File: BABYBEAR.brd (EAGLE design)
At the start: 68.6 x 53.3 mm, 63 parts, among them IC1 ATMEGA1284P, IC2 ATMEGA16U2-MU, IC3 MC33269DT-5.0, IC4 LM358D, IC5 LP2985-33DBVR, J1 Power, J2 Analog, J3 Digital_8_13, J4 Digital_0_7, J5 DC_2_1MM, P1 USB-6PSMT, P2 ICSP:MAIN, P3 ICSP:USB, Q1 FDN340P, Q2 2N7002, X1 16MHz, X2 16MHz

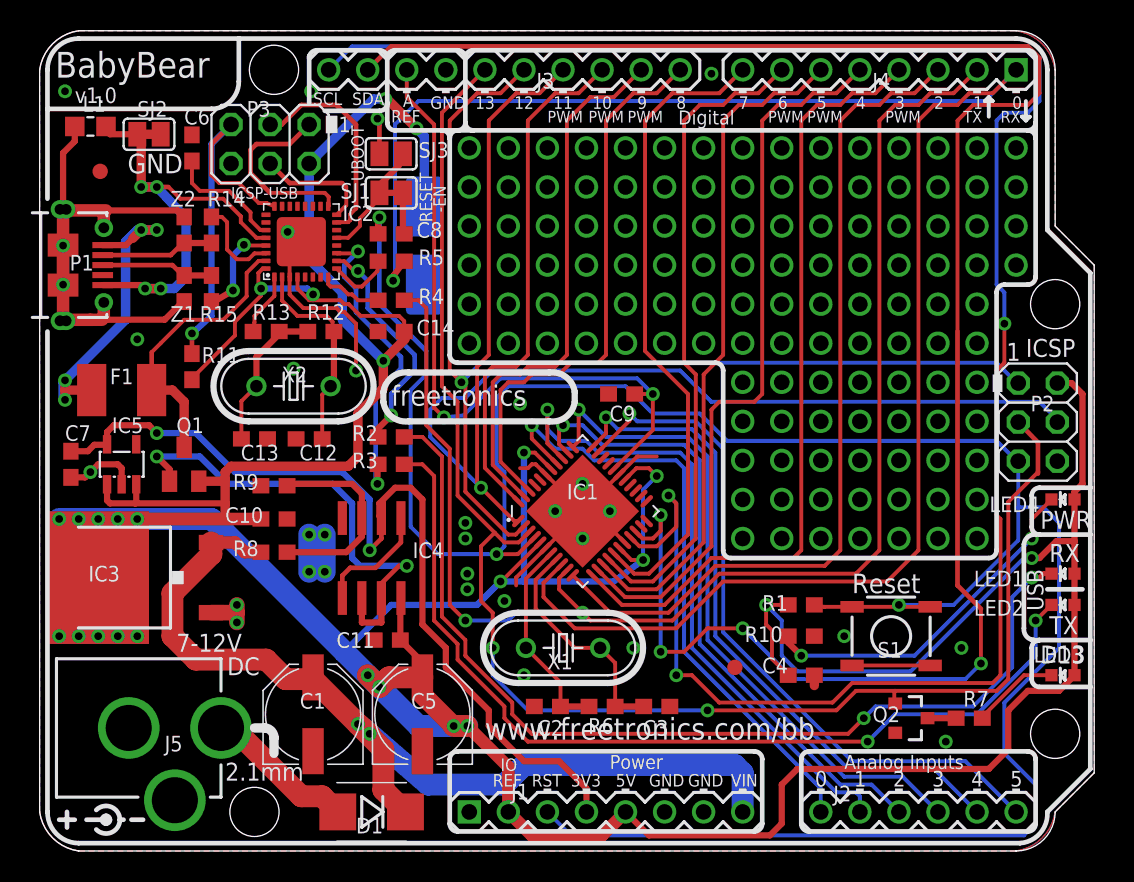
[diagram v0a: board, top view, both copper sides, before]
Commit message: Changed USB connector to USB-C for v2.0 release
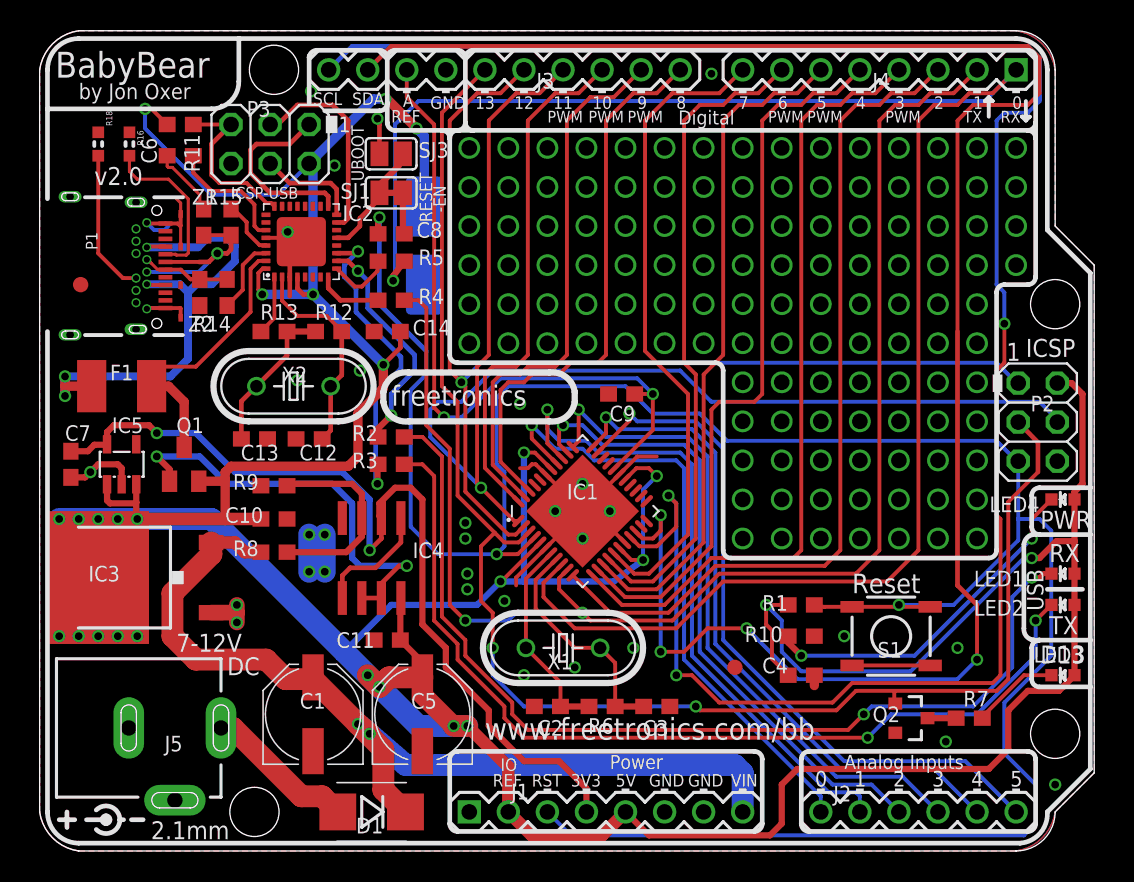
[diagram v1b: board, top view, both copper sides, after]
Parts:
- removed L1: 0805 INDUCTOR, freetronics-master-v1:0805-LARGE
- removed SJ2: GROUND, jumper:SJ
- added R16, R18: 5.1K, freetronics-original:0603
- J5: device freetronics:POWER_JACK_PTH -> freetronics-jon:POWER_JACK_PTH_SLOTS
- P1: value USB-6PSMT -> USB-C; device freetronics-jon:USB-MICROB-MB05PMXX -> freetronics-jon:USB-C-U52A
- moved R11 15.8 mm to (9.14, 47.2), turned to 180 degrees
- moved U$5 7.47 mm to (2.67, 36.8)
- moved P1 7.06 mm to (7.62, 41.7)
- moved R15 4.50 mm to (12.4, 40.9), turned to 270 degrees
- moved Z1 4.50 mm to (10.7, 40.9), turned to 90 degrees
- moved R14 4.19 mm to (12.2, 36.3), turned to 90 degrees
- moved Z2 4.19 mm to (10.4, 36.3), turned to 270 degrees
- moved C6 0.92 mm to (9.14, 45.2), turned to 180 degrees
- moved R13 0.51 mm to (15.2, 33.8)
- moved R12 0.51 mm to (18.8, 33.8)
- moved C14 0.25 mm to (22.6, 33.8)
- moved F1 0.25 mm to (5.33, 30.2)
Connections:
- removed net N$115: F1.1, P1.VBUS
- removed net N$16: P1.D+, R15.2, Z1.1
- removed net N$17: P1.D-, R14.2, Z2.1
- removed net UGND: IC2.28, L1.2, P1.GND, SJ2.1
- new net D+: P1.A6, P1.B6, R15.2, Z1.1
- new net D-: P1.A7, P1.B7, R14.2, Z2.1
- new net N$7: P1.A5, R16.2
- new net USB+: F1.1, P1.A4, P1.A9, P1.B4, P1.B9
- net GND: now also IC2.28, P1.A1, P1.A12, P1.B1, P1.B12, P1.CASE1, P1.CASE2, P1.CASE3, P1.CASE4, P1.FIX1, P1.FIX2, P1.FIX3, P1.FIX4, R16.1, R18.1, Z1.2, Z2.2; no longer SJ2.2
- net N$3: now also P1.B5, R18.2; no longer L1.1, P1.FIX1, P1.FIX2, P1.PIN1, P1.PIN2, P1.TAB1, P1.TAB2, Z1.2, Z2.2
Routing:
- net USB+: track 0.00 -> 33.5 mm, vias 0 -> 2
- net UGND: track 30.9 -> 0.00 mm, vias 4 -> 0
- net N$3: track 34.2 -> 9.48 mm, vias 2 -> 0
- net N$115: track 21.4 -> 0.00 mm, vias 4 -> 0
- net RESET2: track 24.7 -> 11.2 mm, vias 1 -> 0
- net D+: track 0.00 -> 12.4 mm, vias 0 -> 1
- net GND: track 55.3 -> 66.6 mm, vias 30 -> 31
- net N$7: track 0.00 -> 10.7 mm
- net N$17: track 7.40 -> 0.00 mm
- net N$16: track 7.36 -> 0.00 mm
- net D-: track 0.00 -> 5.75 mm
- net 5V: track 300.1 -> 296.4 mm, vias 17 -> 18
- net N$12: track 30.9 -> 27.7 mm
- net RD+: track 6.31 -> 3.64 mm, vias 2 -> 0
- net N$116: track 1.52 -> 0.00 mm
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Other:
- board text added: "by Jon Oxer"
- board text added: "v2.0"
- board text removed: "v1.0"
